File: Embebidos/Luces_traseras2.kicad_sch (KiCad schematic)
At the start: 8 parts, among them J10 RJ45, Q4 BSS138, Q5 DMP3056LSDQ-13

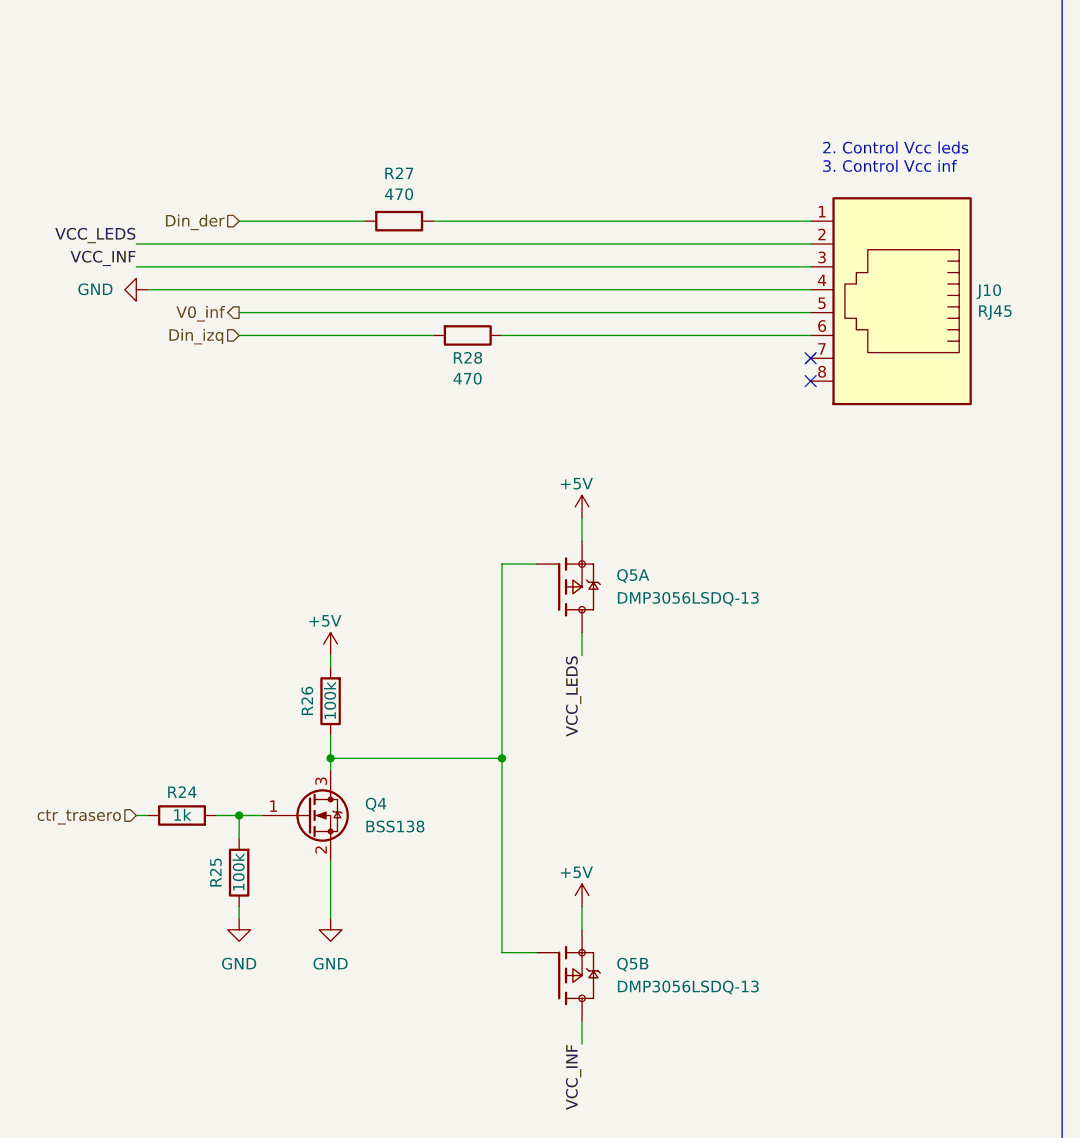
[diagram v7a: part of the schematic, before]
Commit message: Cambios varios
-Conectores movidos a nueva hoja jerarquica

-Transistores DMP colocados en lices delanteras

-Jumpers ubicados para el uso del pin IO13 para SIM800 y LEDHW

-Etiqueta de "no conectado" ubicada en USB_UART
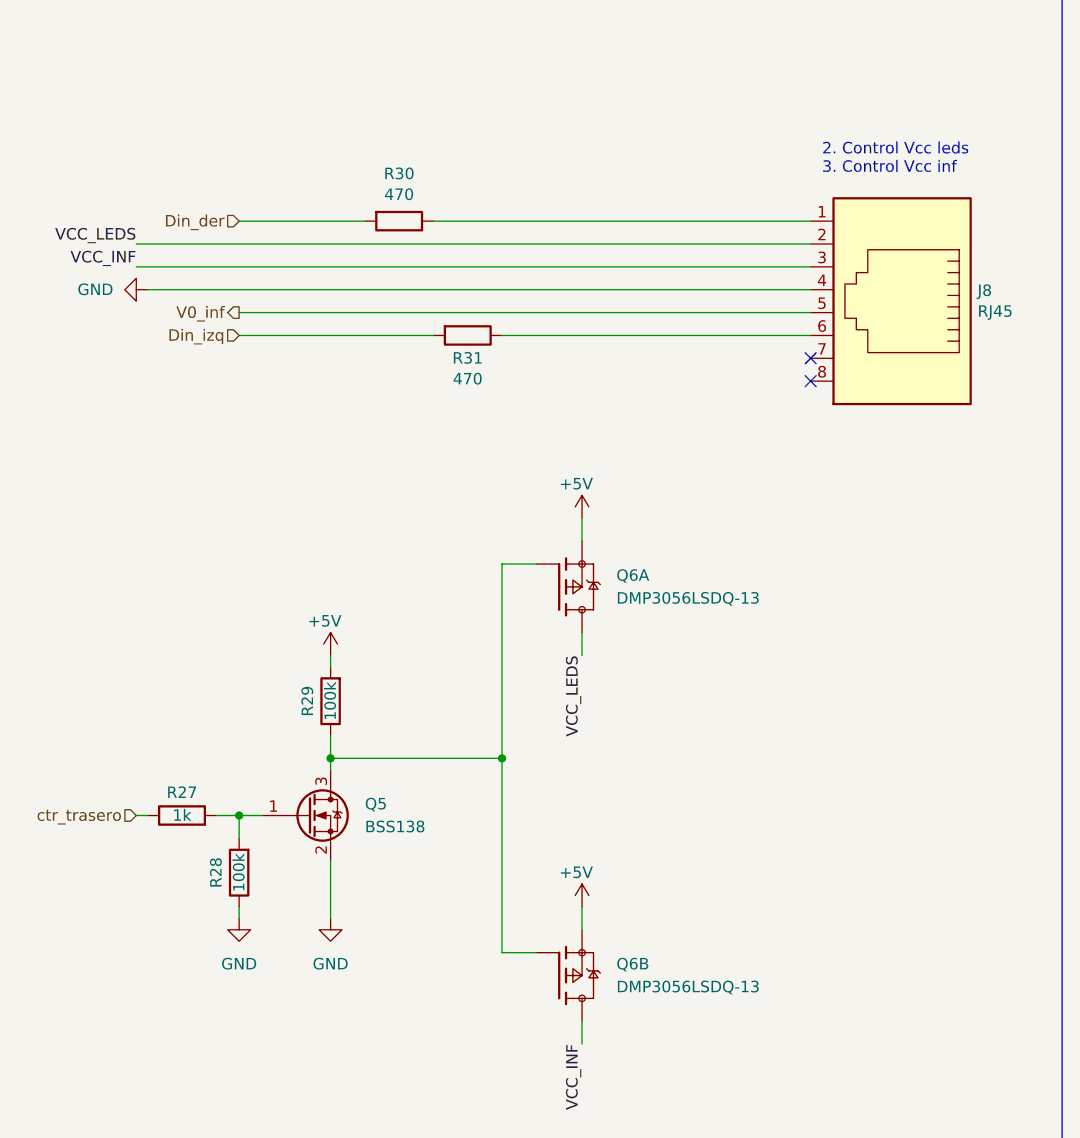
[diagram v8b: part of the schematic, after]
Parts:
- renumbered J10 to J8, Q4 to Q5, Q5 to Q6, R24 to R27, R25 to R28, R26 to R29, R27 to R30, R28 to R31
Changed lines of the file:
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@@
   (symbol (lib_id "Device:R") (at 55.88 83.82 270) (unit 1)
     (in_bom yes) (on_board yes)
-    (property "Reference" "R27" (id 0) (at 55.88 78.5622 90))
+    (property "Reference" "R30" (id 0) (at 55.88 78.5622 90))
     (property "Value" "470" (id 1) (at 55.88 80.8736 90))
     (property "Footprint" "" (id 2) (at 55.88 82.042 90)
@@
   (symbol (lib_id "Device:R") (at 63.5 96.52 270) (unit 1)
     (in_bom yes) (on_board yes)
-    (property "Reference" "R28" (id 0) (at 63.5 99.06 90))
+    (property "Reference" "R31" (id 0) (at 63.5 99.06 90))
     (property "Value" "470" (id 1) (at 63.5 101.3714 90))
     (property "Footprint" "" (id 2) (at 63.5 94.742 90)
@@
   (symbol (lib_id "Connector:RJ45") (at 111.76 91.44 180) (unit 1)
     (in_bom yes) (on_board yes)
-    (property "Reference" "J10" (id 0) (at 120.142 91.5416 0)
+    (property "Reference" "J8" (id 0) (at 120.142 91.5416 0)
       (effects (font (size 1.27 1.27)) (justify right))
     )
@@
   (symbol (lib_id "Device:R") (at 31.75 149.86 90) (unit 1)
     (in_bom yes) (on_board yes)
-    (property "Reference" "R24" (id 0) (at 31.75 147.32 90))
+    (property "Reference" "R27" (id 0) (at 31.75 147.32 90))
     (property "Value" "1k" (id 1) (at 31.75 149.86 90))
     (property "Footprint" "" (id 2) (at 31.75 151.638 90)
@@
   (symbol (lib_id "Transistor_FET:BSS138") (at 45.72 149.86 0) (unit 1)
     (in_bom yes) (on_board yes) (fields_autoplaced)
-    (property "Reference" "Q4" (id 0) (at 52.07 148.5899 0)
+    (property "Reference" "Q5" (id 0) (at 52.07 148.5899 0)
       (effects (font (size 1.27 1.27)) (justify left))
     )
@@
   (symbol (lib_id "Device:R") (at 48.26 137.16 180) (unit 1)
     (in_bom yes) (on_board yes)
-    (property "Reference" "R26" (id 0) (at 45.72 137.16 90))
+    (property "Reference" "R29" (id 0) (at 45.72 137.16 90))
     (property "Value" "100k" (id 1) (at 48.26 137.16 90))
     (property "Footprint" "" (id 2) (at 50.038 137.16 90)
@@
   (symbol (lib_id "Device:R") (at 38.1 156.21 180) (unit 1)
     (in_bom yes) (on_board yes)
-    (property "Reference" "R25" (id 0) (at 35.56 156.21 90))
+    (property "Reference" "R28" (id 0) (at 35.56 156.21 90))
     (property "Value" "100k" (id 1) (at 38.1 156.21 90))
     (property "Footprint" "" (id 2) (at 39.878 156.21 90)
@@
   (symbol (lib_id "DMP3056LSDQ-13:DMP3056LSDQ-13") (at 73.66 124.46 0) (unit 1)
     (in_bom yes) (on_board yes) (fields_autoplaced)
-    (property "Reference" "Q5" (id 0) (at 80.01 123.1899 0)
+    (property "Reference" "Q6" (id 0) (at 80.01 123.1899 0)
       (effects (font (size 1.27 1.27)) (justify left))
     )
@@
   (symbol (lib_id "DMP3056LSDQ-13:DMP3056LSDQ-13") (at 73.66 167.64 0) (unit 2)
     (in_bom yes) (on_board yes) (fields_autoplaced)
-    (property "Reference" "Q5" (id 0) (at 80.01 166.3699 0)
-      (effects (font (size 1.27 1.27)) (justify left))
-    )
+    (property "Reference" "Q6" (id 0) (at 80.01 166.3699 0)
+      (effects (font (size 1.27 1.27)) (justify left))
+    )
